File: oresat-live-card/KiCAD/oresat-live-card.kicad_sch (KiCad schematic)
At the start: 0 parts

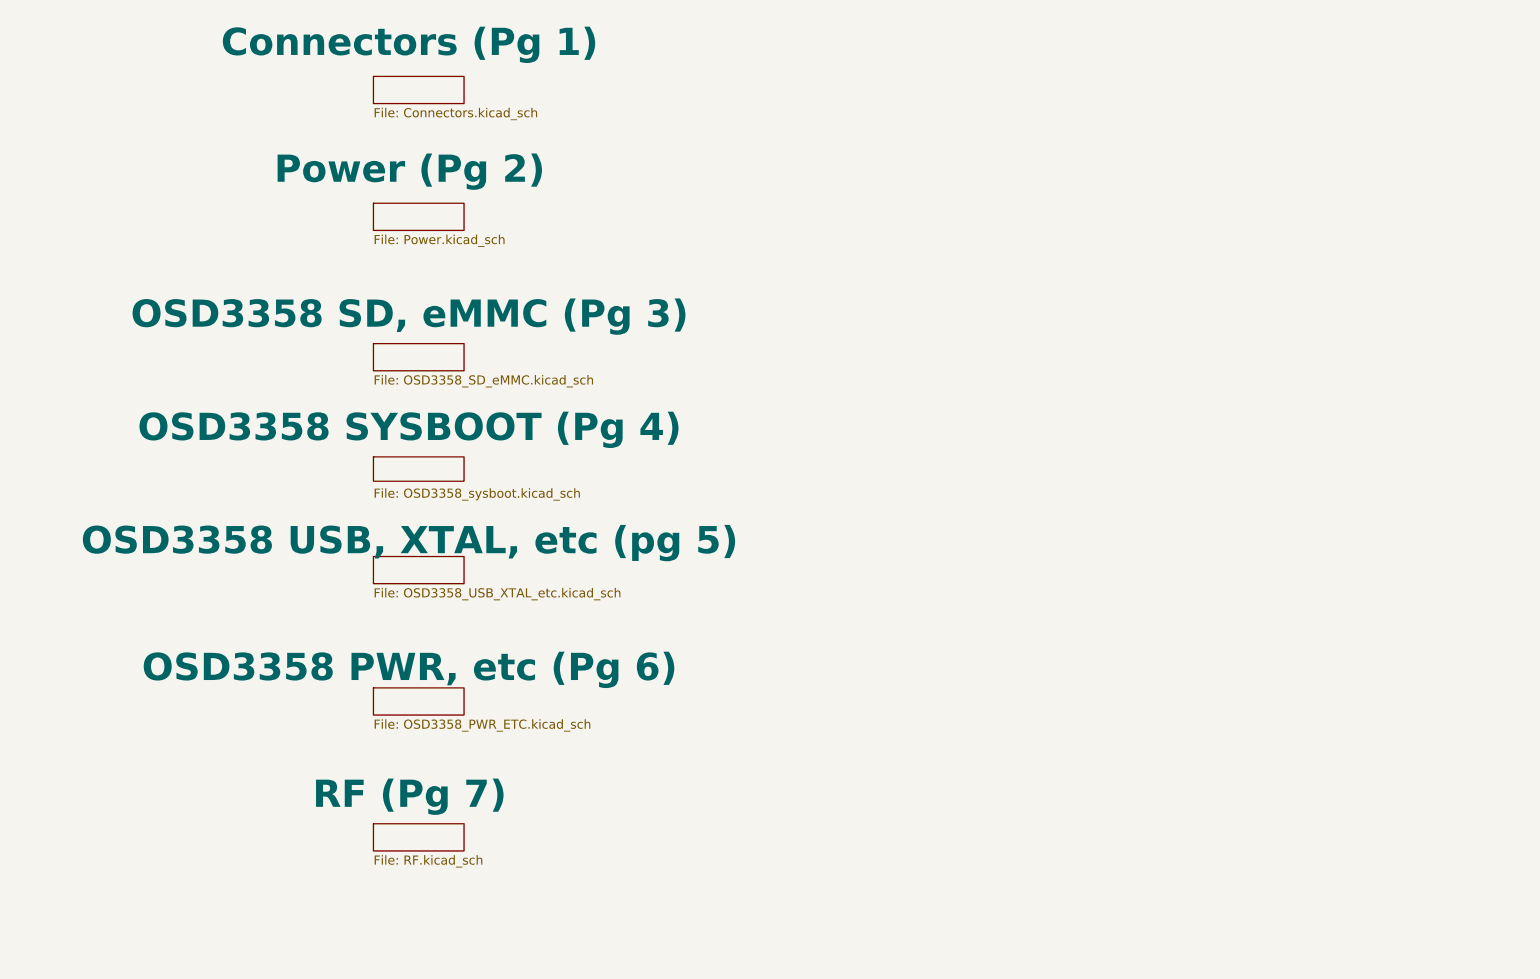
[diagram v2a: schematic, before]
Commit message: added new sheets for LNA and switching
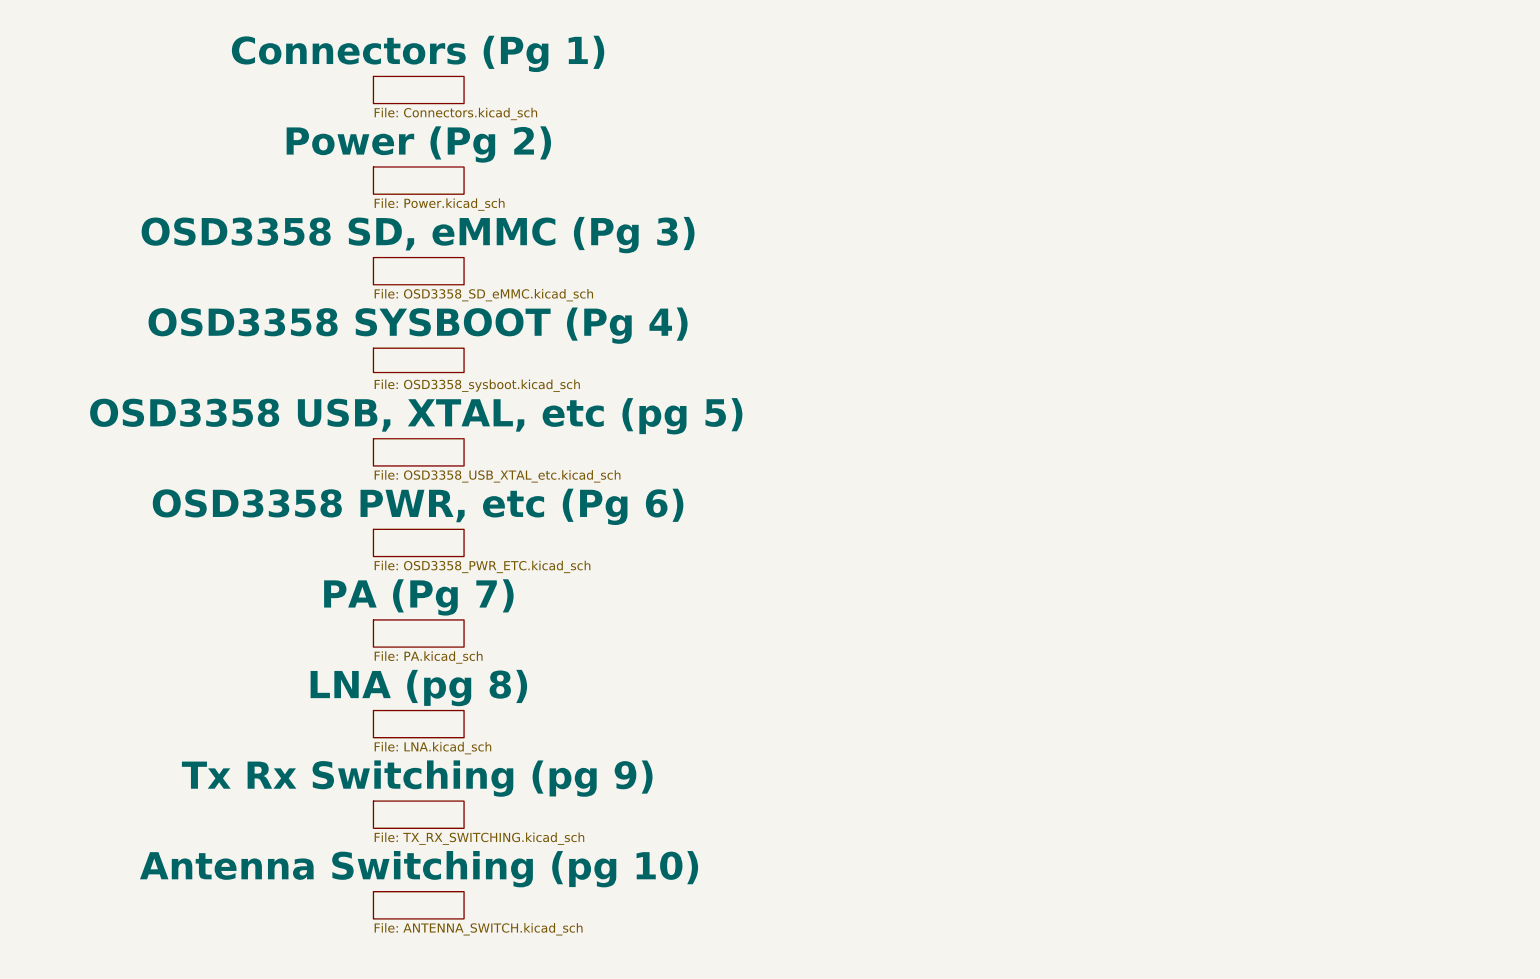
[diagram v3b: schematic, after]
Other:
- sheet RF (Pg 7) renamed PA (Pg 7)
- added sheet Antenna Switching (pg 10) (ANTENNA_SWITCH.kicad_sch)
- added sheet LNA (pg 8) (LNA.kicad_sch)
- added sheet Tx Rx Switching (pg 9) (TX_RX_SWITCHING.kicad_sch)
- sheet PA (Pg 7): file RF.kicad_sch -> PA.kicad_sch
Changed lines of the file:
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@@
 (kicad_sch
-	(version 20231120)
+	(version 20250114)
 	(generator "eeschema")
-	(generator_version "8.0")
+	(generator_version "9.0")
 	(paper "B")
 	(title_block
@@
 	)
 	(sheet
-		(at 101.6 142.875)
-		(size 12.7 3.81)
-		(stroke
-			(width 0)
-			(type solid)
-		)
-		(fill
-			(color 0 0 0 0.0000)
-		)
-		(property "Sheetname" "RF (Pg 7)"
-			(at 106.68 140.97 0)
-			(effects
-				(font
-					(size 3.81 3.81)
-					(bold yes)
-				)
-				(justify bottom)
-			)
-		)
-		(property "Sheetfile" "RF.kicad_sch"
-			(at 101.6 147.2696 0)
+		(at 101.6 114.3)
+		(size 12.7 3.81)
+		(exclude_from_sim no)
+		(in_bom yes)
+		(on_board yes)
+		(dnp no)
+		(stroke
+			(width 0)
+			(type solid)
+		)
+		(fill
+			(color 0 0 0 0.0000)
+		)
+		(property "Sheetname" "PA (Pg 7)"
+			(at 107.95 113.03 0)
+			(effects
+				(font
+					(size 3.81 3.81)
+					(bold yes)
+				)
+				(justify bottom)
+			)
+		)
+		(property "Sheetfile" "PA.kicad_sch"
+			(at 101.6 118.6946 0)
 			(effects
 				(font
@@
 		(at 101.6 38.1)
 		(size 12.7 3.81)
+		(exclude_from_sim no)
+		(in_bom yes)
+		(on_board yes)
+		(dnp no)
 		(stroke
 			(width 0)
@@
 		)
 		(property "Sheetname" "Connectors (Pg 1)"
-			(at 106.68 35.56 0)
+			(at 107.95 36.83 0)
 			(effects
 				(font
@@
 	)
 	(sheet
-		(at 101.6 105.41)
-		(size 12.7 3.81)
+		(at 101.6 88.9)
+		(size 12.7 3.81)
+		(exclude_from_sim no)
+		(in_bom yes)
+		(on_board yes)
+		(dnp no)
 		(stroke
 			(width 0)
@@
 		)
 		(property "Sheetname" "OSD3358 USB, XTAL, etc (pg 5)"
-			(at 106.68 105.41 0)
+			(at 107.696 87.63 0)
 			(effects
 				(font
@@
 		)
 		(property "Sheetfile" "OSD3358_USB_XTAL_etc.kicad_sch"
-			(at 101.6 109.8046 0)
+			(at 101.6 93.2946 0)
 			(effects
 				(font
@@
 	)
 	(sheet
-		(at 101.6 75.565)
-		(size 12.7 3.81)
+		(at 101.6 63.5)
+		(size 12.7 3.81)
+		(exclude_from_sim no)
+		(in_bom yes)
+		(on_board yes)
+		(dnp no)
 		(stroke
 			(width 0)
@@
 		)
 		(property "Sheetname" "OSD3358 SD, eMMC (Pg 3)"
-			(at 106.68 73.66 0)
+			(at 107.95 62.23 0)
 			(effects
 				(font
@@
 		)
 		(property "Sheetfile" "OSD3358_SD_eMMC.kicad_sch"
-			(at 101.6 79.9596 0)
+			(at 101.6 67.8946 0)
 			(effects
 				(font
@@
 	)
 	(sheet
-		(at 101.6 91.44)
+		(at 101.6 76.2)
 		(size 12.7 3.413)
+		(exclude_from_sim no)
+		(in_bom yes)
+		(on_board yes)
+		(dnp no)
 		(stroke
 			(width 0)
@@
 		)
 		(property "Sheetname" "OSD3358 SYSBOOT (Pg 4)"
-			(at 106.68 89.535 0)
+			(at 107.95 74.93 0)
 			(effects
 				(font
@@
 		)
 		(property "Sheetfile" "OSD3358_sysboot.kicad_sch"
-			(at 101.6 95.8346 0)
+			(at 101.6 80.5946 0)
 			(effects
 				(font
@@
 	)
 	(sheet
-		(at 101.6 123.825)
-		(size 12.7 3.81)
+		(at 101.6 139.7)
+		(size 12.7 3.81)
+		(exclude_from_sim no)
+		(in_bom yes)
+		(on_board yes)
+		(dnp no)
+		(stroke
+			(width 0.1524)
+			(type solid)
+		)
+		(fill
+			(color 0 0 0 0.0000)
+		)
+		(property "Sheetname" "Tx Rx Switching (pg 9)"
+			(at 107.95 138.43 0)
+			(effects
+				(font
+					(size 3.81 3.81)
+					(thickness 0.762)
+					(bold yes)
+				)
+				(justify bottom)
+			)
+		)
+		(property "Sheetfile" "TX_RX_SWITCHING.kicad_sch"
+			(at 101.6 144.0946 0)
+			(effects
+				(font
+					(size 1.27 1.27)
+				)
+				(justify left top)
+			)
+		)
+		(instances
+			(project "oresat-live-card"
+				(path "/748bdd2d-da0a-4240-ba60-0bf881d2ec56"
+					(page "9")
+				)
+			)
+		)
+	)
+	(sheet
+		(at 101.6 101.6)
+		(size 12.7 3.81)
+		(exclude_from_sim no)
+		(in_bom yes)
+		(on_board yes)
+		(dnp no)
 		(stroke
 			(width 0)
@@
 		)
 		(property "Sheetname" "OSD3358 PWR, etc (Pg 6)"
-			(at 106.68 123.19 0)
+			(at 107.95 100.33 0)
 			(effects
 				(font
@@
 		)
 		(property "Sheetfile" "OSD3358_PWR_ETC.kicad_sch"
-			(at 101.6 128.2196 0)
+			(at 101.6 105.9946 0)
 			(effects
 				(font
@@
 	)
 	(sheet
-		(at 101.6 55.88)
-		(size 12.7 3.81)
+		(at 101.6 50.8)
+		(size 12.7 3.81)
+		(exclude_from_sim no)
+		(in_bom yes)
+		(on_board yes)
+		(dnp no)
 		(stroke
 			(width 0)
@@
 		)
 		(property "Sheetname" "Power (Pg 2)"
-			(at 106.68 53.34 0)
+			(at 107.95 49.53 0)
 			(effects
 				(font
@@
 		)
 		(property "Sheetfile" "Power.kicad_sch"
-			(at 101.6 60.2746 0)
+			(at 101.6 55.1946 0)
 			(effects
 				(font
@@
 				(path "/748bdd2d-da0a-4240-ba60-0bf881d2ec56"
 					(page "2")
+				)
+			)
+		)
+	)
+	(sheet
+		(at 101.6 127)
+		(size 12.7 3.81)
+		(exclude_from_sim no)
+		(in_bom yes)
+		(on_board yes)
+		(dnp no)
+		(stroke
+			(width 0.1524)
+			(type solid)
+		)
+		(fill
+			(color 0 0 0 0.0000)
+		)
+		(property "Sheetname" "LNA (pg 8)"
+			(at 107.95 125.73 0)
+			(effects
+				(font
+					(size 3.81 3.81)
+					(thickness 0.762)
+					(bold yes)
+				)
+				(justify bottom)
+			)
+		)
+		(property "Sheetfile" "LNA.kicad_sch"
+			(at 101.6 131.3946 0)
+			(effects
+				(font
+					(size 1.27 1.27)
+				)
+				(justify left top)
+			)
+		)
+		(instances
+			(project "oresat-live-card"
+				(path "/748bdd2d-da0a-4240-ba60-0bf881d2ec56"
+					(page "8")
+				)
+			)
+		)
+	)
+	(sheet
+		(at 101.6 152.4)
+		(size 12.7 3.81)
+		(exclude_from_sim no)
+		(in_bom yes)
+		(on_board yes)
+		(dnp no)
+		(stroke
+			(width 0.1524)
+			(type solid)
+		)
+		(fill
+			(color 0 0 0 0.0000)
+		)
+		(property "Sheetname" "Antenna Switching (pg 10)"
+			(at 108.204 151.13 0)
+			(effects
+				(font
+					(size 3.81 3.81)
+					(thickness 0.762)
+					(bold yes)
+				)
+				(justify bottom)
+			)
+		)
+		(property "Sheetfile" "ANTENNA_SWITCH.kicad_sch"
+			(at 101.6 156.7946 0)
+			(effects
+				(font
+					(size 1.27 1.27)
+				)
+				(justify left top)
+			)
+		)
+		(instances
+			(project "oresat-live-card"
+				(path "/748bdd2d-da0a-4240-ba60-0bf881d2ec56"
+					(page "10")
 				)
 			)
@@
 		)
 	)
+	(embedded_fonts no)
 )

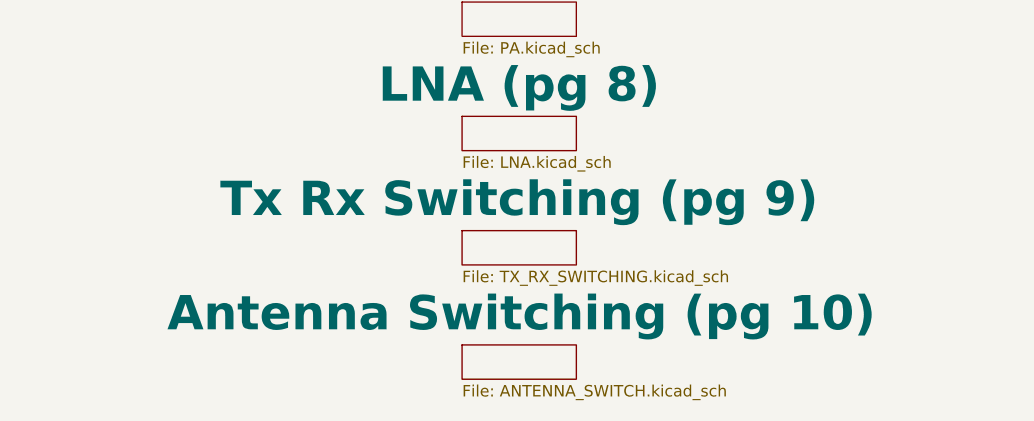
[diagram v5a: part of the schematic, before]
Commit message: updated sheet numbering and title, merged antenna switching and tx rx switching sheets
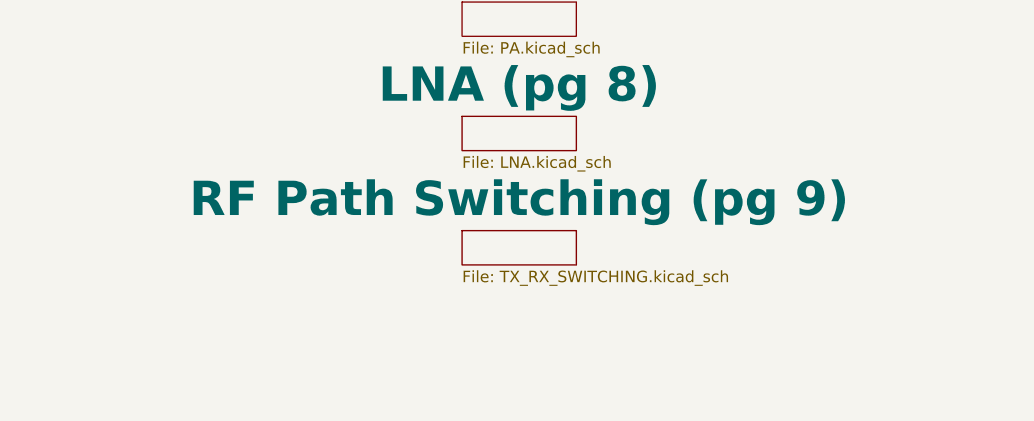
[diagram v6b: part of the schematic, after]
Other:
- sheet Tx Rx Switching (pg 9) renamed RF Path Switching (pg 9)
- removed sheet Antenna Switching (pg 10)
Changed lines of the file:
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@@
 	(title_block
 		(title "Oresat DxWifi Card")
-		(date "2025-05-28")
+		(date "2025-07-06")
 		(rev "2")
 	)
@@
 			(color 0 0 0 0.0000)
 		)
-		(property "Sheetname" "Tx Rx Switching (pg 9)"
+		(property "Sheetname" "RF Path Switching (pg 9)"
 			(at 107.95 138.43 0)
 			(effects
@@
 				)
 			)
-		)
-	)
-	(sheet
-		(at 101.6 152.4)
-		(size 12.7 3.81)
-		(exclude_from_sim no)
-		(in_bom yes)
-		(on_board yes)
-		(dnp no)
-		(stroke
-			(width 0.1524)
-			(type solid)
-		)
-		(fill
-			(color 0 0 0 0.0000)
-		)
-		(property "Sheetname" "Antenna Switching (pg 10)"
-			(at 108.204 151.13 0)
-			(effects
-				(font
-					(size 3.81 3.81)
-					(thickness 0.762)
-					(bold yes)
-				)
-				(justify bottom)
-			)
-		)
-		(property "Sheetfile" "ANTENNA_SWITCH.kicad_sch"
-			(at 101.6 156.7946 0)
-			(effects
-				(font
-					(size 1.27 1.27)
-				)
-				(justify left top)
-			)
-		)
-		(instances
-			(project "oresat-live-card"
-				(path "/748bdd2d-da0a-4240-ba60-0bf881d2ec56"
-					(page "10")
-				)
-			)

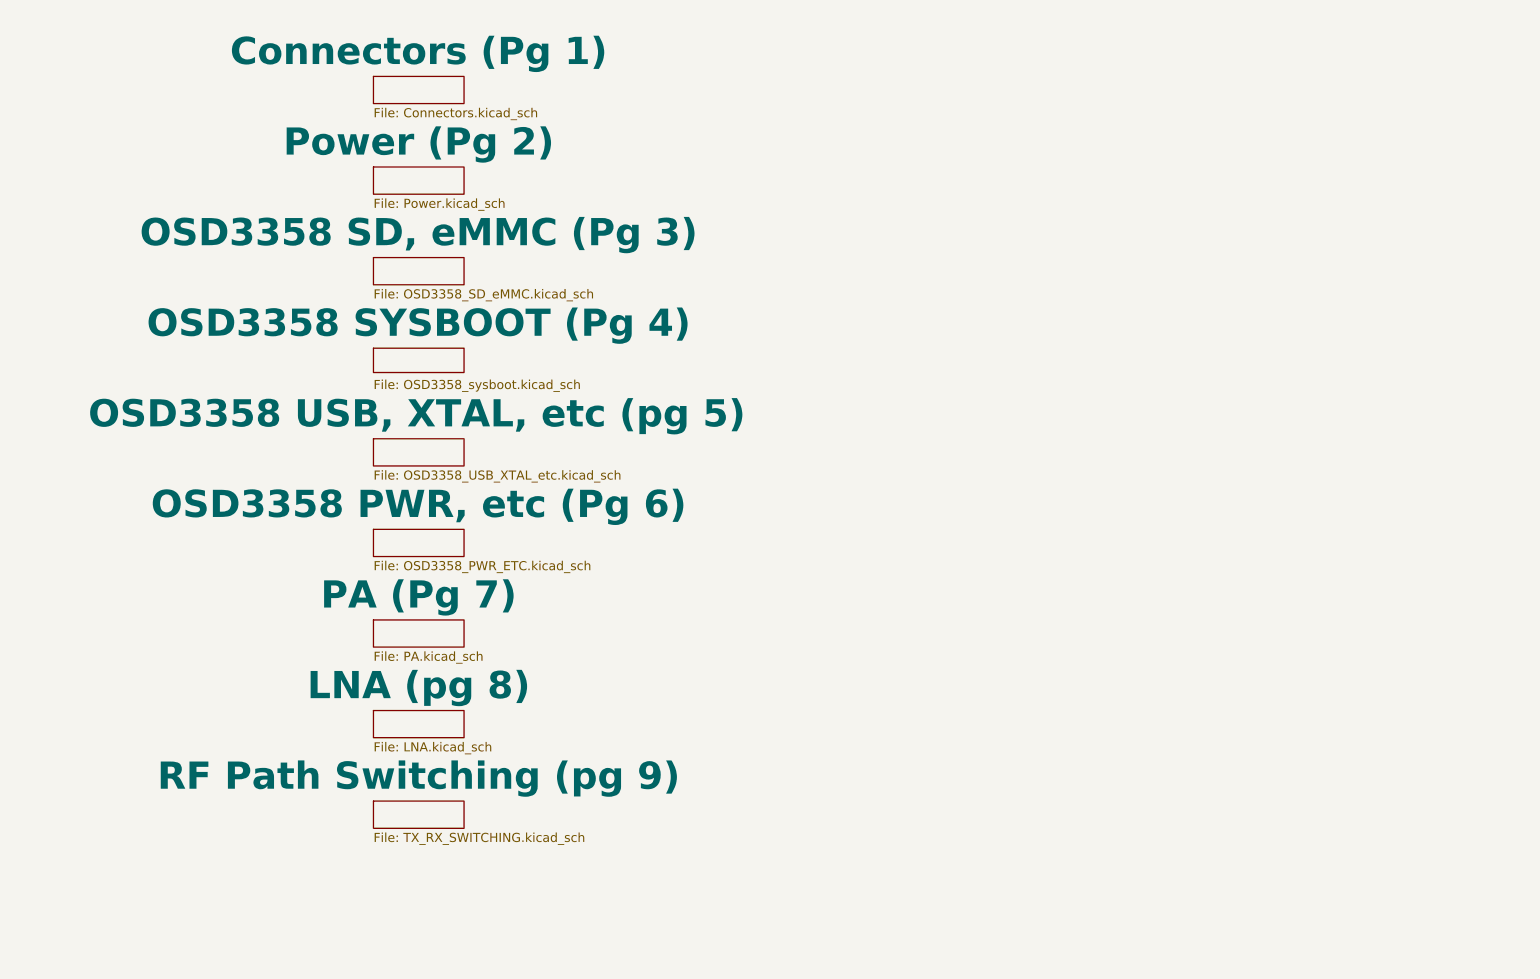
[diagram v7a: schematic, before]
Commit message: CLeaned up main connector, page names to be consistent with Octavo designs, sanity checks.
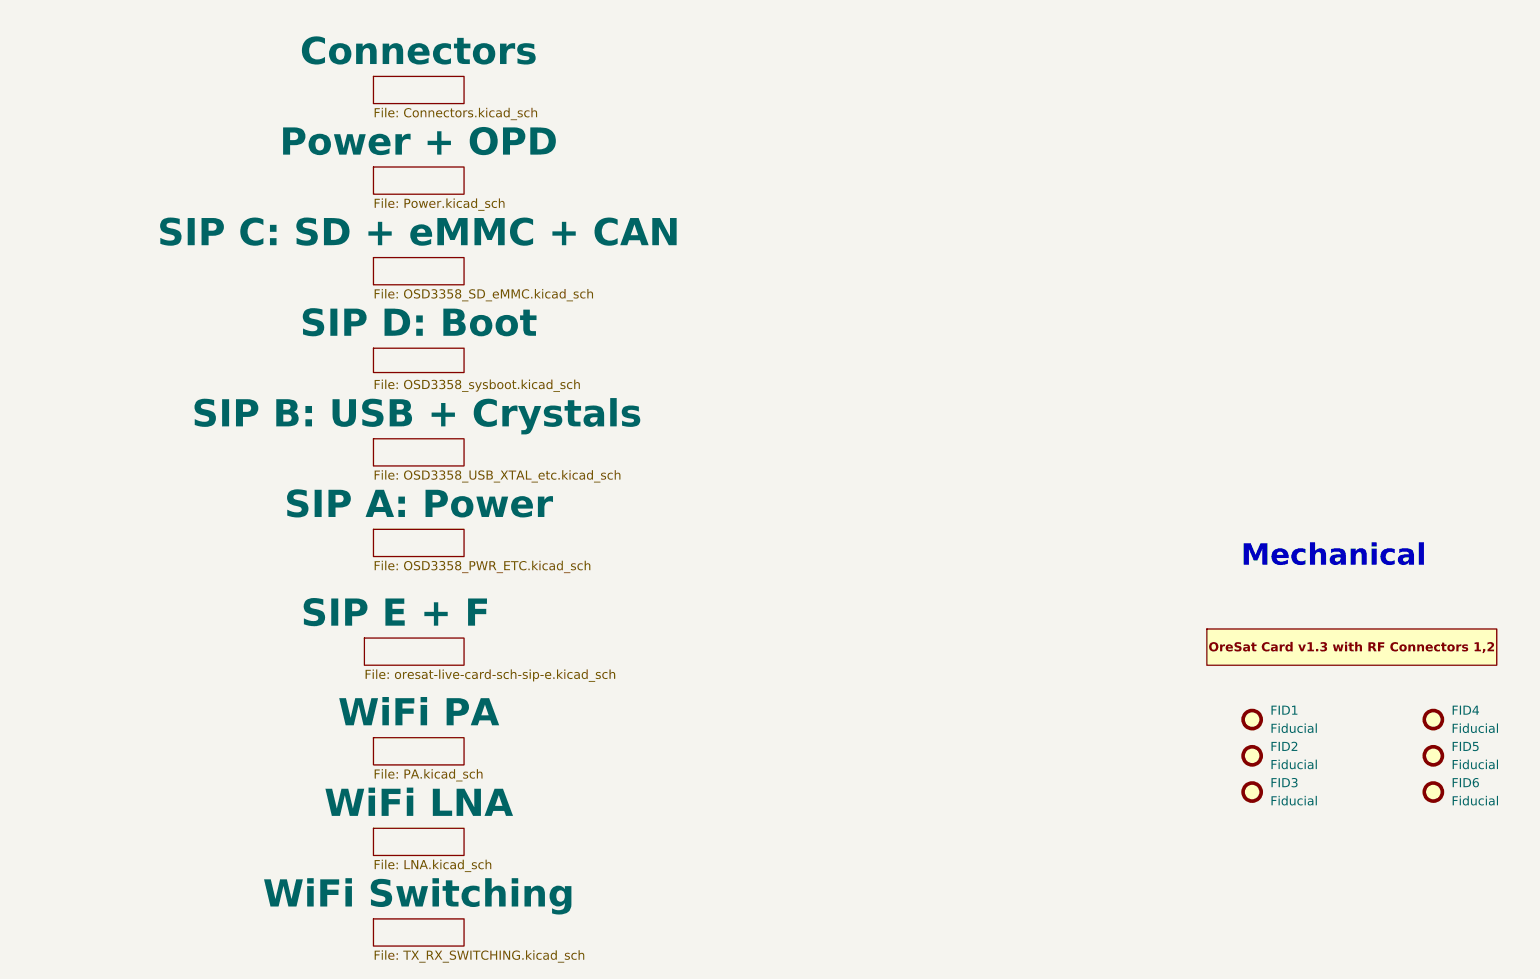
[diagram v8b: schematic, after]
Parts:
- added FID1, FID2, FID3, FID4, FID5, FID6: Fiducial, Fiducial:Fiducial_1mm_Mask2mm, symbol Mechanical:Fiducial
- added PCB1: ORESAT-CARD-V1.3-GENERIC-1RF-POS1, oresat-pcbs:ORESAT-CARD-V1.3-2RF-LEFT, symbol oresat-pcbs:ORESAT-CARD-V1.3-2RF-LEFT
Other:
- sheet Connectors (Pg 1) renamed Connectors
- sheet LNA (pg 8) renamed WiFi LNA
- sheet OSD3358 PWR, etc (Pg 6) renamed SIP A: Power
- sheet OSD3358 SD, eMMC (Pg 3) renamed SIP C: SD + eMMC + CAN
- sheet OSD3358 SYSBOOT (Pg 4) renamed SIP D: Boot
- sheet OSD3358 USB, XTAL, etc (pg 5) renamed SIP B: USB + Crystals
- sheet PA (Pg 7) renamed WiFi PA
- sheet Power (Pg 2) renamed Power + OPD
- sheet RF Path Switching (pg 9) renamed WiFi Switching
- added sheet SIP E + F (oresat-live-card-sch-sip-e.kicad_sch)
- note added: "Mechanical"
- title: Oresat DxWifi Card -> Oresat Live Card
